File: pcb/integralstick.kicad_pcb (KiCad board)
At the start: 4 copper layers, 219 parts, among them J1 CONN_INTEGRALSTICK_FPGA_DEVICE, J2 CONN_INTEGRALSTICK_MCU_DEVICE, Q1 SSM6N58NU, Q2 SSM6N58NU, Q3 SSM6N58NU, U1 STM32F777NIH6‎, U10 DSC6083MI2A-032K768, U12 DSC6001HI2A-025.0000‎, U2 XC7A50T-1FTG256C, U3 S27KS0641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

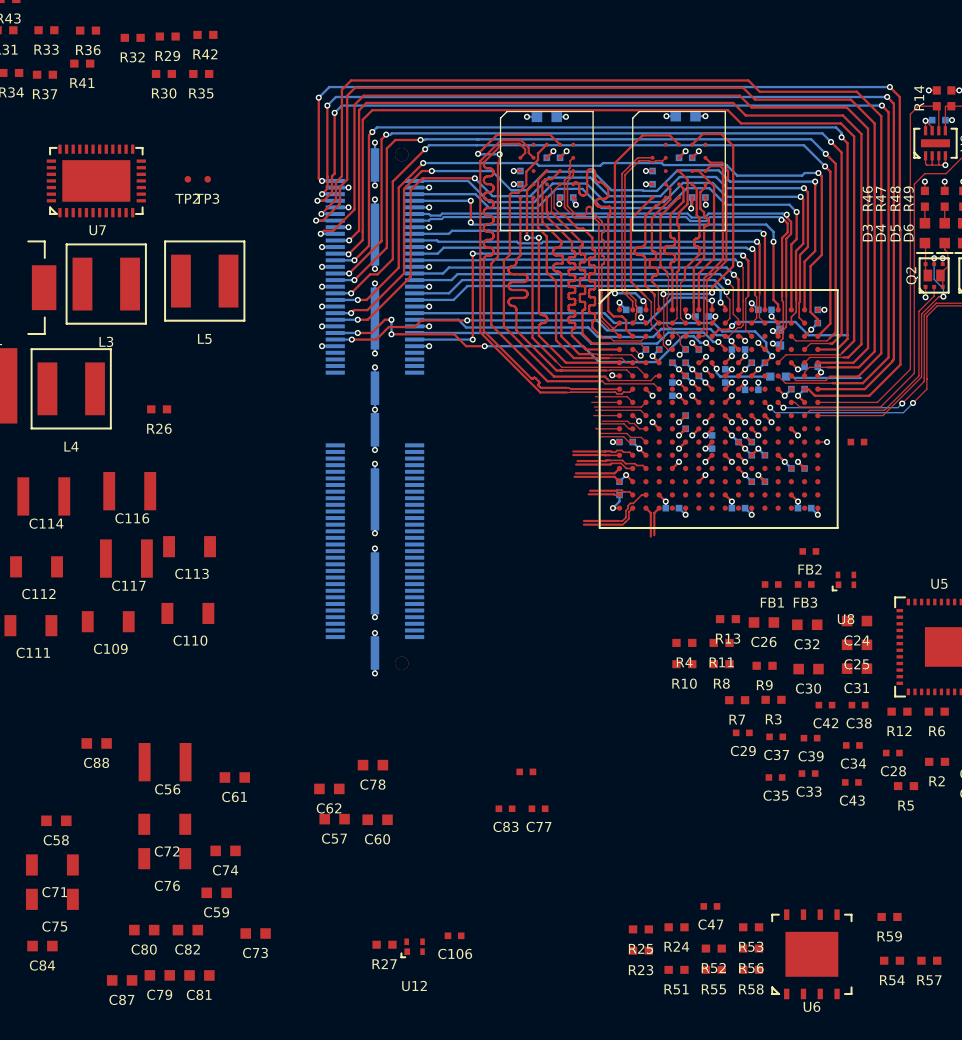
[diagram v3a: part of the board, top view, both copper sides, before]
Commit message: Added layer-change caps by Q-strip
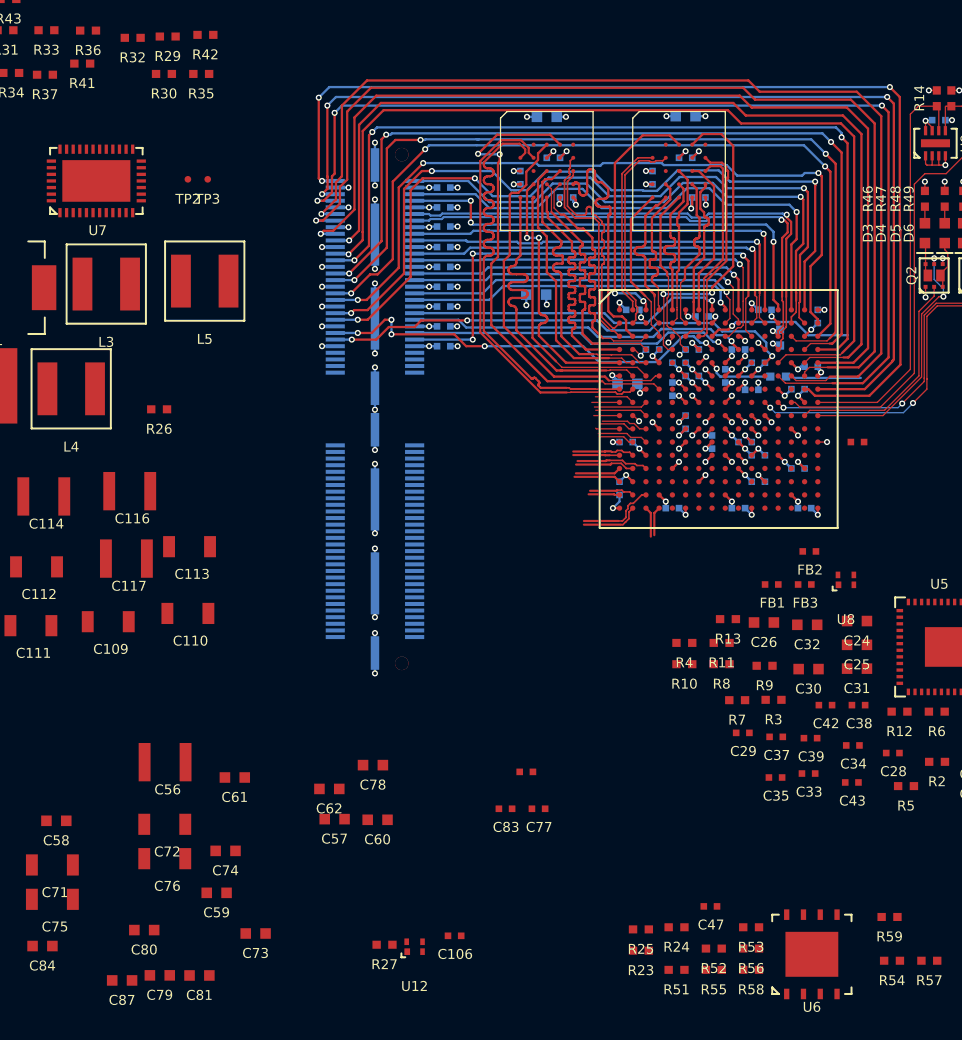
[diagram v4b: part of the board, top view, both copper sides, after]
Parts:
- added C119: 0.47 uF, azonenberg_pcb:EIA_0402_CAP_NOSILK, B.Cu at (43.2, 26.2)
- added C120: 0.47 uF, azonenberg_pcb:EIA_0402_CAP_NOSILK, B.Cu at (43.2, 27.8)
- added C121: 0.47 uF, azonenberg_pcb:EIA_0402_CAP_NOSILK, B.Cu at (43.2, 35.2)
- added C122: 0.47 uF, azonenberg_pcb:EIA_0402_CAP_NOSILK, B.Cu at (43.2, 29.2)
- added C123: 0.47 uF, azonenberg_pcb:EIA_0402_CAP_NOSILK, B.Cu at (43.2, 36.8)
- added C124: 0.47 uF, azonenberg_pcb:EIA_0402_CAP_NOSILK, B.Cu at (43.2, 38.2)
- added C125: 0.47 uF, azonenberg_pcb:EIA_0402_CAP_NOSILK, B.Cu at (43.2, 30.8)
- added C126: 0.47 uF, azonenberg_pcb:EIA_0402_CAP_NOSILK, B.Cu at (43.2, 33.8)
- added C127: 0.47 uF, azonenberg_pcb:EIA_0402_CAP_NOSILK, B.Cu at (43.2, 32.2)
- C82, C88: moved to B.Cu
- moved C82 54.8 mm to (50.2, 34.4)
- moved C88 48.5 mm to (57.1, 41.1)
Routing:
- net /GND: track 317.9 -> 349.1 mm, vias 68 -> 78
- net /1V8: track 98.5 -> 114.2 mm, vias 20 -> 21
- net /3V3: track 188.1 -> 193.3 mm
- net /FPGA/IO_3V3_23: track 79.0 -> 78.3 mm
- net /FPGA/IO_3V3_22: track 76.9 -> 76.2 mm
- net /FPGA/IO_3V3_19: track 71.2 -> 70.5 mm
- net /FPGA/IO_3V3_21: track 73.4 -> 72.8 mm

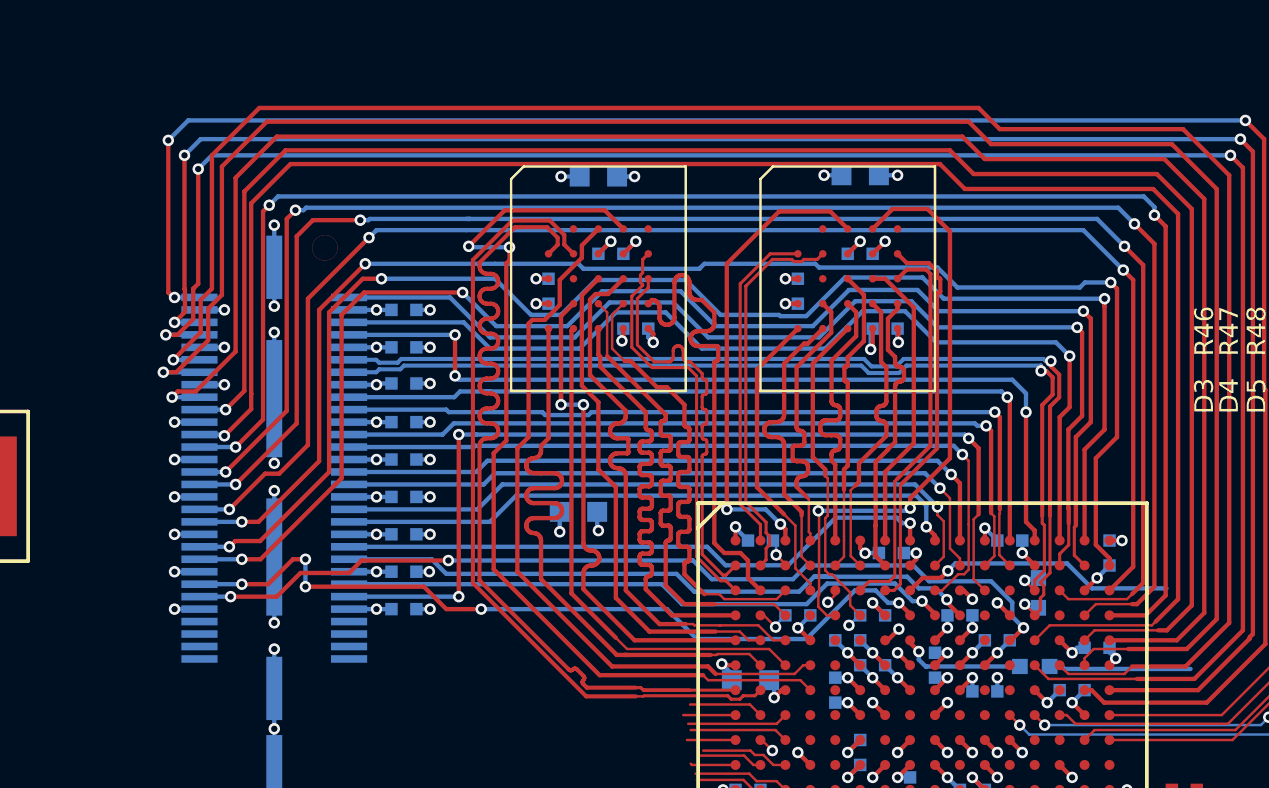
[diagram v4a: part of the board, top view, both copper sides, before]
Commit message: Initial FPGA plane layout
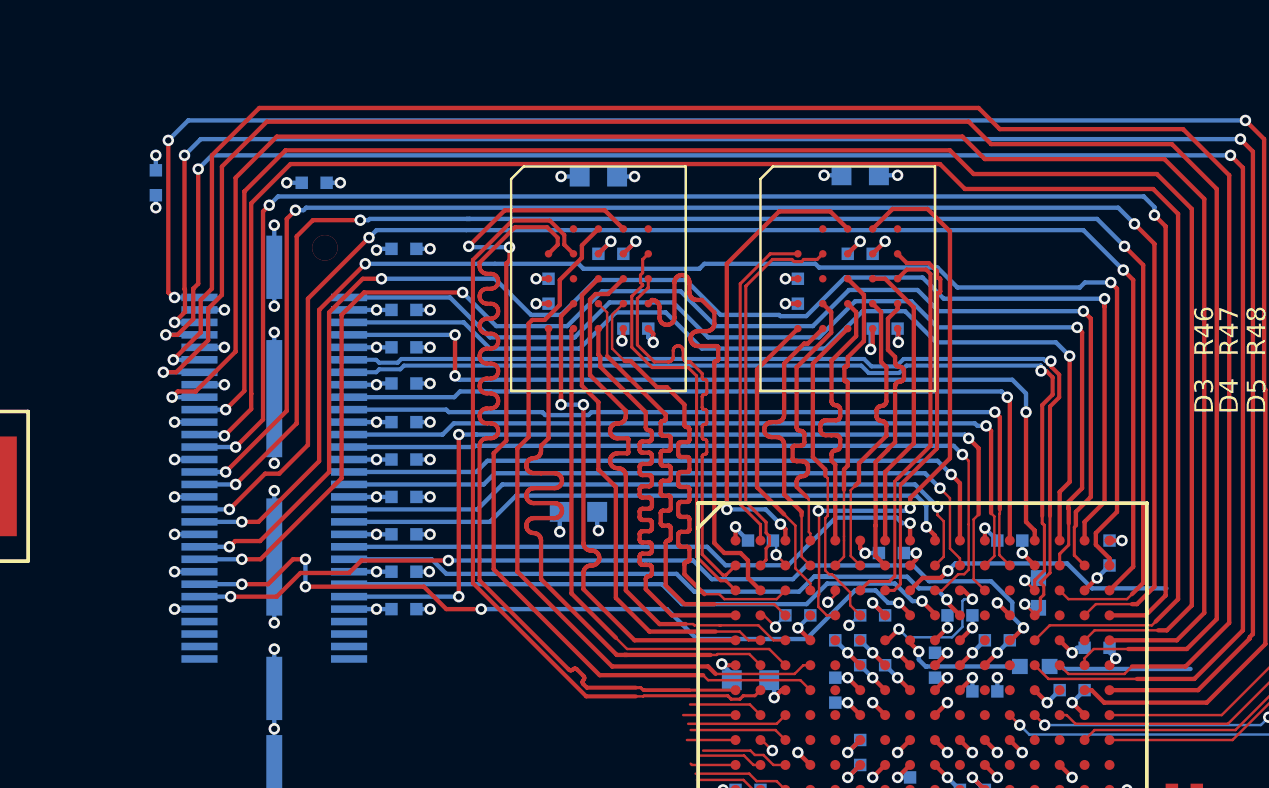
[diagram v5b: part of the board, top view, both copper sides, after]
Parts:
- added C128: 0.47 uF, azonenberg_pcb:EIA_0402_CAP_NOSILK, B.Cu at (43.2, 23.8)
- added C129: 0.47 uF, azonenberg_pcb:EIA_0402_CAP_NOSILK, B.Cu at (39.6, 21.1)
- added C130: 0.47 uF, azonenberg_pcb:EIA_0402_CAP_NOSILK, B.Cu at (33.2, 21.1)
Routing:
- net /GND: track 349.1 -> 364.9 mm, vias 78 -> 81
- net /3V3: track 193.3 -> 182.3 mm, vias 40 -> 43
- net /2V5: track 4.33 -> 12.5 mm
- net /1V8: track 114.2 -> 115.5 mm
- added copper zone on In2.Cu, net /1V0
- added copper zone on In2.Cu, net /1V8
- added copper zone on In2.Cu, net /2V5
- added copper zone on In2.Cu, net /3V3

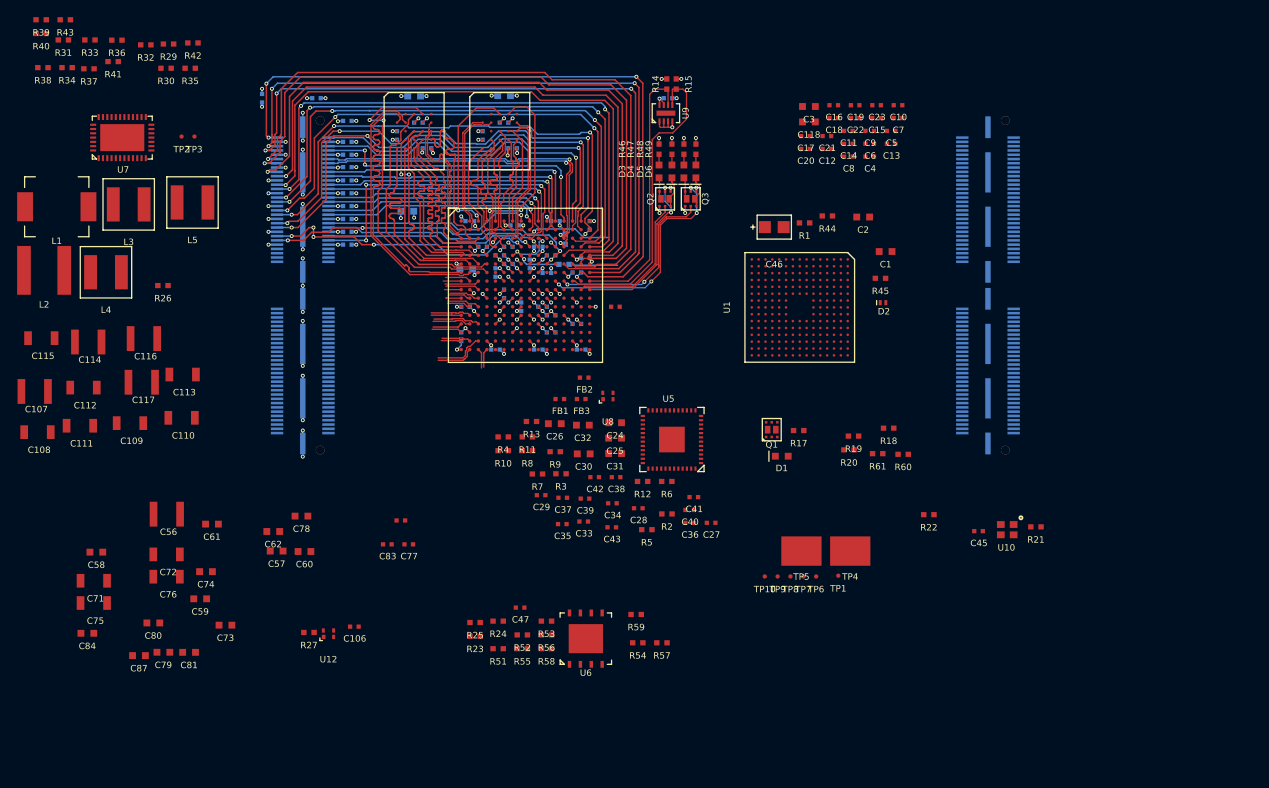
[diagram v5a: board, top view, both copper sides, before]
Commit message: Began work on LVCMOS18 GPIOs. Swapped a lot of pins around.
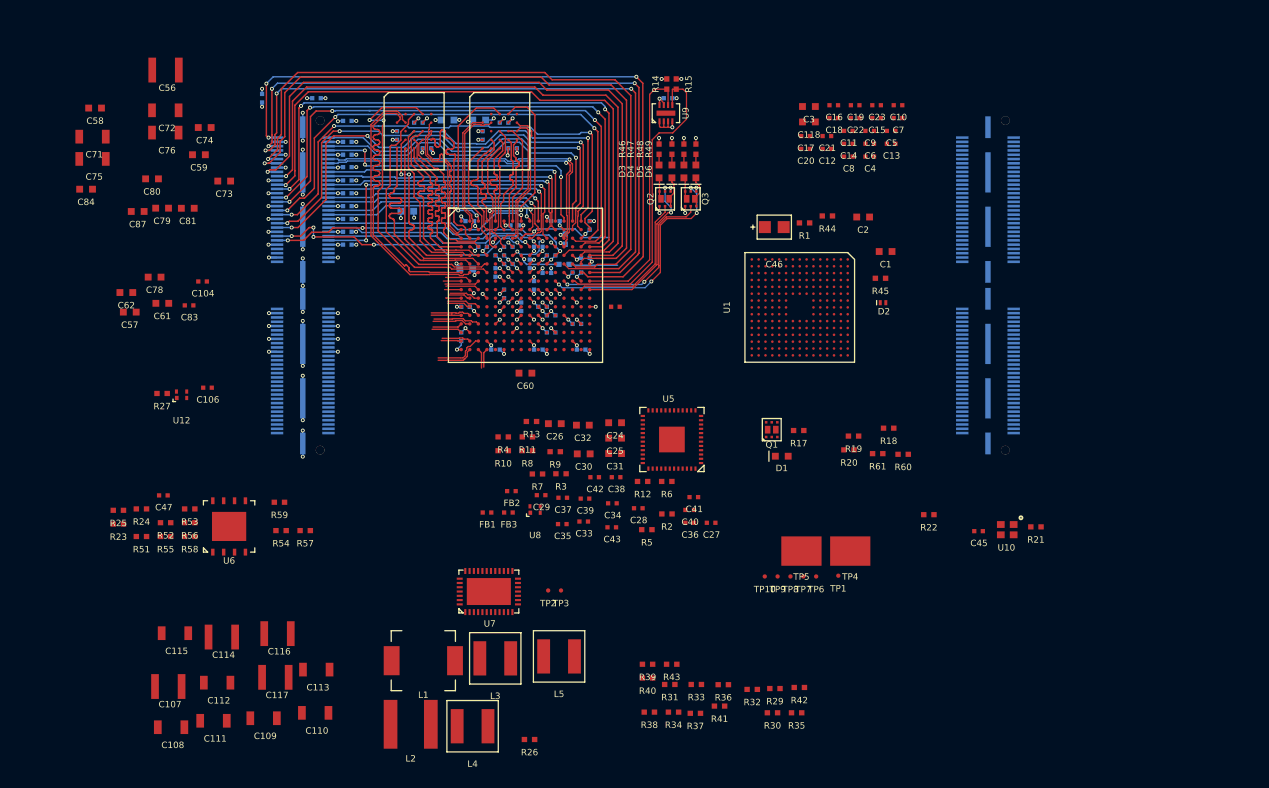
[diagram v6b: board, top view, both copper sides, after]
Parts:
- C77: moved to B.Cu
- moved R29 103.3 mm to (93.1, 90.1)
- moved R30 103.3 mm to (92.8, 92.9)
- moved R31 103.3 mm to (80.8, 89.6)
- moved R32 103.3 mm to (90.5, 90.2)
- moved R33 103.3 mm to (84.0, 89.6)
- moved R34 103.3 mm to (81.3, 92.8)
- moved R35 103.3 mm to (95.7, 92.9)
- moved R36 103.3 mm to (87.1, 89.6)
- moved R37 103.3 mm to (83.8, 93.0)
- moved R38 103.3 mm to (78.5, 92.8)
- moved R39 103.3 mm to (78.3, 87.2)
- moved R40 103.3 mm to (78.3, 88.8)
- moved R41 103.3 mm to (86.7, 92.1)
- moved R42 103.3 mm to (96.0, 90.0)
- moved R43 103.3 mm to (81.1, 87.2)
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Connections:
- J1 pad 1: /1V8 -> /Power Supply/5V0
- J1 pad 10: /RAM/GPIO_1V8_5 -> /FPGA/LVDS_DQ4_N
- J1 pad 11: /RAM/GPIO_1V8_6 -> /FPGA/LVDS_DQ2_P
- J1 pad 12: /RAM/GPIO_1V8_7 -> /FPGA/LVDS_DQ2_N
- J1 pad 13: /1V8 -> /2V5
- J1 pad 14: /1V8 -> /2V5
- J1 pad 15: /RAM/GPIO_1V8_8 -> /FPGA/LVDS_DQ8_P
- J1 pad 16: /RAM/GPIO_1V8_9 -> /FPGA/GPIO_2V5_0
- J1 pad 17: /RAM/GPIO_1V8_10 -> /FPGA/LVDS_DQ8_N
- J1 pad 18: /RAM/GPIO_1V8_11 -> /FPGA/GPIO_2V5_1
- J1 pad 19: /1V8 -> /2V5
- J1 pad 2: /1V8 -> /2V5
- J1 pad 20: /1V8 -> /2V5
- J1 pad 21: /RAM/GPIO_1V8_12 -> /FPGA/LVDS_DQ6_P
- J1 pad 22: /RAM/GPIO_1V8_13 -> /FPGA/LVDS_DQ5_P
- J1 pad 23: /RAM/GPIO_1V8_14 -> /FPGA/LVDS_DQ6_N
- J1 pad 24: /RAM/GPIO_1V8_15 -> /FPGA/LVDS_DQ5_N
- J1 pad 26: /1V8 -> /2V5
- J1 pad 27: /RAM/GPIO_1V8_16 -> /FPGA/LVDS_DQ7_P
- J1 pad 28: /RAM/GPIO_1V8_17 -> /FPGA/LVDS_DQ7_N
- J1 pad 29: /RAM/CLK_1V8_0 -> /FPGA/LVDS_DQ3_N
- J1 pad 3: /RAM/GPIO_1V8_0 -> /2V5
- J1 pad 30: /RAM/CLK_1V8_1 -> /FPGA/LVDS_DQ3_P
- J1 pad 31: /1V8 -> /2V5
- J1 pad 32: /1V8 -> /2V5
- J1 pad 33: /2V5 -> /1V8
- J1 pad 39: /2V5 -> /1V8
- J1 pad 4: /RAM/GPIO_1V8_1 -> /Power Supply/5V0
- J1 pad 40: /2V5 -> /1V8
- J1 pad 41: /FPGA/LVDS_DQ2_P -> /RAM/GPIO_1V8_16
- J1 pad 42: /FPGA/LVDS_DQ3_N -> /RAM/CLK_1V8_0
- J1 pad 43: /FPGA/LVDS_DQ2_N -> /RAM/GPIO_1V8_17
- J1 pad 44: /FPGA/LVDS_DQ3_P -> /RAM/CLK_1V8_1
- J1 pad 45: /2V5 -> /1V8
- J1 pad 46: /2V5 -> /1V8
- J1 pad 47: /FPGA/LVDS_DQ4_P -> /RAM/GPIO_1V8_15
- J1 pad 48: /FPGA/LVDS_DQ5_P -> /RAM/GPIO_1V8_14
- J1 pad 49: /FPGA/LVDS_DQ4_N -> /RAM/GPIO_1V8_13
- J1 pad 5: /RAM/GPIO_1V8_2 -> /Power Supply/5V0
- J1 pad 50: /FPGA/LVDS_DQ5_N -> /RAM/GPIO_1V8_12
- J1 pad 51: /2V5 -> /1V8
- J1 pad 52: /2V5 -> /1V8
- J1 pad 53: /FPGA/LVDS_DQ6_P -> /RAM/GPIO_1V8_11
- J1 pad 54: /FPGA/LVDS_DQ7_P -> /RAM/GPIO_1V8_10
- J1 pad 55: /FPGA/LVDS_DQ6_N -> /RAM/GPIO_1V8_9
- J1 pad 56: /FPGA/LVDS_DQ7_N -> /RAM/GPIO_1V8_8
- J1 pad 57: /2V5 -> /1V8
- J1 pad 58: /2V5 -> /1V8
- J1 pad 59: /Power Supply/5V0 -> /RAM/GPIO_1V8_7
- J1 pad 6: /RAM/GPIO_1V8_3 -> /Power Supply/5V0
- J1 pad 60: /Power Supply/5V0 -> /RAM/GPIO_1V8_6
- J1 pad 61: /Power Supply/5V0 -> /RAM/GPIO_1V8_5
- J1 pad 62: /Power Supply/5V0 -> /RAM/GPIO_1V8_4
- J1 pad 63: /2V5 -> /1V8
- J1 pad 64: /2V5 -> /1V8
- J1 pad 65: /FPGA/LVDS_DQ8_P -> /RAM/GPIO_1V8_3
- J1 pad 66: /FPGA/GPIO_2V5_0 -> /RAM/GPIO_1V8_2
- J1 pad 67: /FPGA/LVDS_DQ8_N -> /RAM/GPIO_1V8_1
- J1 pad 68: /FPGA/GPIO_2V5_1 -> /RAM/GPIO_1V8_0
- J1 pad 7: /1V8 -> /2V5
- J1 pad 8: /1V8 -> /2V5
- J1 pad 9: /RAM/GPIO_1V8_4 -> /FPGA/LVDS_DQ4_P
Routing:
- net /1V8: track 115.5 -> 158.5 mm, vias 21 -> 31
- net /GND: track 364.9 -> 356.9 mm
- net /FPGA/IO_3V3_5: track 57.5 -> 56.7 mm
- net /1V0: track 30.1 -> 30.6 mm
